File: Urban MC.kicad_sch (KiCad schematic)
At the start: 78 parts, among them J1 Conn_01x02, J2 Conn_01x02, J3 Conn_01x03, J4 Conn_01x02, Q1 IQE022N06LM5CGSCATMA1, Q10 IQE022N06LM5CGSCATMA1, Q11 IQE022N06LM5CGSCATMA1, Q12 IQE022N06LM5CGSCATMA1, Q13 IQE022N06LM5CGSCATMA1, Q14 IQE022N06LM5CGSCATMA1, Q15 IQE022N06LM5CGSCATMA1, Q16 IQE022N06LM5CGSCATMA1, Q17 IQE022N06LM5CGSCATMA1, Q18 IQE022N06LM5CGSCATMA1, Q19 IQE022N06LM5CGSCATMA1, Q2 IQE022N06LM5CGSCATMA1, Q20 IQE022N06LM5CGSCATMA1, Q21 IQE022N06LM5CGSCATMA1, Q22 IQE022N06LM5CGSCATMA1, Q23 IQE022N06LM5CGSCATMA1, Q24 IQE022N06LM5CGSCATMA1, Q3 IQE022N06LM5CGSCATMA1, Q4 IQE022N06LM5CGSCATMA1, Q5 IQE022N06LM5CGSCATMA1, Q6 IQE022N06LM5CGSCATMA1, Q7 IQE022N06LM5CGSCATMA1, Q8 IQE022N06LM5CGSCATMA1, Q9 IQE022N06LM5CGSCATMA1, SW1 CAN_TERM, SW2 SW_Push, U1 MCP2561/2, U1 MCP4725, U2 MCP2515-xSO, Y1 8MHz

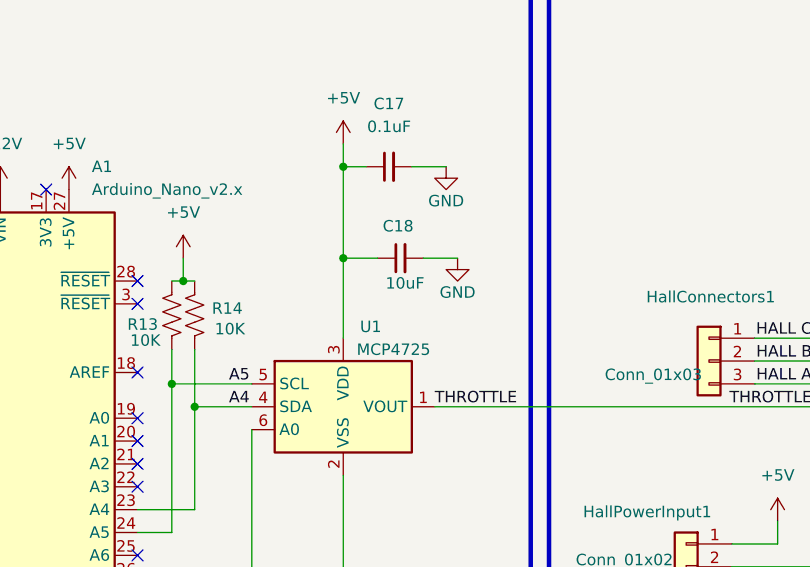
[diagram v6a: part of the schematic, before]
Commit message: all datasheets except CAN TERM and crystal
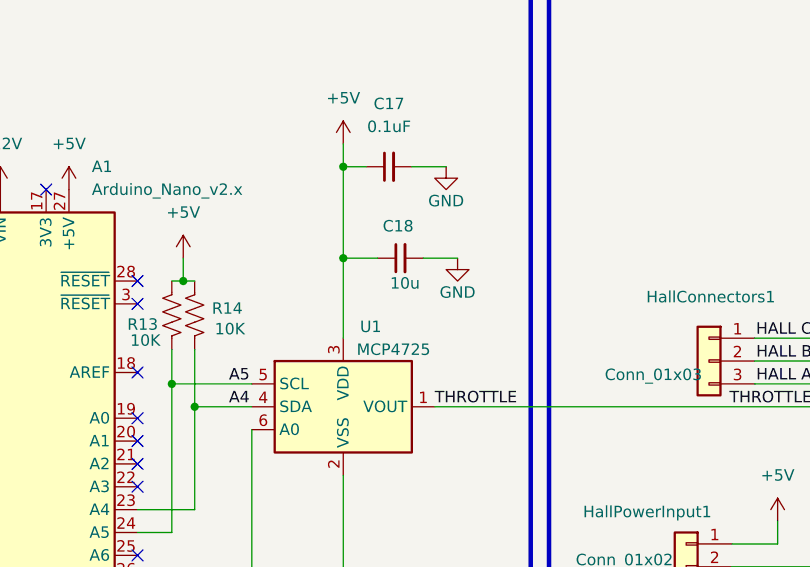
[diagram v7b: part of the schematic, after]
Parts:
- C18: value 10uF -> 10u; footprint Capacitor_SMD:C_0805_2012Metric_Pad1.18x1.45mm_HandSolder -> Capacitor_SMD:C_0805_2012Metric
- R4: footprint Resistor_SMD:R_0805_2012Metric_Pad1.20x1.40mm_HandSolder -> Resistor_SMD:R_0402_1005Metric
- SW2: footprint Button_Switch_THT:SW_PUSH_6mm -> urban_mc_custom_footprints:SW_TS04-66-70-BK-160-SMT
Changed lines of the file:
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@@
 			)
 		)
-		(property "Datasheet" "~"
+		(property "Datasheet" "https://www.molex.com/content/dam/molex/molex-dot-com/products/automated/en-us/salesdrawingpdf/436/43650/436500200_sd.pdf?inline"
 			(at 97.79 58.42 0)
 			(effects
@@
 			)
 		)
-		(property "Footprint" "Button_Switch_THT:SW_PUSH_6mm"
+		(property "Footprint" "urban_mc_custom_footprints:SW_TS04-66-70-BK-160-SMT"
 			(at 250.19 74.93 0)
 			(effects
@@
 			)
 		)
-		(property "Datasheet" "~"
+		(property "Datasheet" "https://www.sameskydevices.com/product/resource/ts04.pdf"
 			(at 250.19 74.93 0)
 			(effects
@@
 			)
 		)
-		(property "Datasheet" "~"
+		(property "Datasheet" "https://www.molex.com/content/dam/molex/molex-dot-com/products/automated/en-us/salesdrawingpdf/436/43650/436500200_sd.pdf?inline"
 			(at 201.93 102.87 0)
 			(effects
@@
 			)
 		)
-		(property "Datasheet" "~"
+		(property "Datasheet" "https://search.murata.co.jp/Ceramy/image/img/A01X/G101/ENG/GRM21BR61H106KE43-01A.pdf"
 			(at 308.61 72.39 0)
 			(effects
@@
 			)
 		)
-		(property "Datasheet" "~"
+		(property "Datasheet" "https://www.seielect.com/catalog/sei-rmcf_rmcp.pdf"
 			(at 76.2 59.69 0)
 			(effects
@@
 			)
 		)
-		(property "Datasheet" "~"
+		(property "Datasheet" "https://www.te.com/usa-en/product-1986660-2.datasheet.pdf"
 			(at 26.67 179.07 0)
 			(effects
@@
 			)
 		)
-		(property "Datasheet" "~"
+		(property "Datasheet" "https://search.murata.co.jp/Ceramy/image/img/A01X/G101/ENG/GRM21BR61H106KE43-01A.pdf"
 			(at 308.61 171.45 0)
 			(effects
@@
 			)
 		)
-		(property "Footprint" "Resistor_SMD:R_0805_2012Metric_Pad1.20x1.40mm_HandSolder"
+		(property "Footprint" "Resistor_SMD:R_0402_1005Metric"
 			(at 49.149 78.994 90)
 			(effects
@@
 			)
 		)
-		(property "Datasheet" "~"
+		(property "Datasheet" "https://industrial.panasonic.com/cdbs/www-data/pdf/RDA0000/AOA0000C304.pdf"
 			(at 48.895 80.01 0)
 			(effects
@@
 			)
 		)
-		(property "Datasheet" "~"
+		(property "Datasheet" "https://search.murata.co.jp/Ceramy/image/img/A01X/G101/ENG/GRM21BR61H106KE43-01A.pdf"
 			(at 308.61 123.19 0)
 			(effects
@@
 			)
 		)
-		(property "Datasheet" "~"
+		(property "Datasheet" "https://www.digikey.ca/en/products/detail/vishay-dale/CRCW040211R0FKED/1177783"
 			(at 313.69 67.31 0)
 			(effects
@@
 			)
 		)
-		(property "Datasheet" "~"
+		(property "Datasheet" "https://search.murata.co.jp/Ceramy/image/img/A01X/G101/ENG/GRM21BR61H106KE43-01A.pdf"
 			(at 285.75 165.1 0)
 			(effects
@@
 			)
 		)
-		(property "Datasheet" "~"
+		(property "Datasheet" "https://www.digikey.ca/en/products/detail/vishay-dale/CRCW040211R0FKED/1177783"
 			(at 308.61 82.55 0)
 			(effects
@@
 			)
 		)
-		(property "Value" "10uF"
+		(property "Value" "10u"
 			(at 170.688 73.914 90)
 			(effects
@@
 			)
 		)
-		(property "Footprint" "Capacitor_SMD:C_0805_2012Metric_Pad1.18x1.45mm_HandSolder"
+		(property "Footprint" "Capacitor_SMD:C_0805_2012Metric"
 			(at 170.18 71.12 0)
 			(effects
@@
 			)
 		)
-		(property "Datasheet" "https://search.murata.co.jp/Ceramy/image/img/A01X/G101/ENG/GRM21BR61C106KE15-01.pdf"
+		(property "Datasheet" "https://search.murata.co.jp/Ceramy/image/img/A01X/G101/ENG/GRM21BR61H106KE43-01A.pdf"
 			(at 170.18 71.12 0)
 			(effects
@@
 			)
 		)
-		(property "Datasheet" "~"
+		(property "Datasheet" "https://www.digikey.ca/en/products/detail/vishay-dale/CRCW040211R0FKED/1177783"
 			(at 313.69 118.11 0)
 			(effects
@@
 			)
 		)
-		(property "Datasheet" "~"
+		(property "Datasheet" "https://www.seielect.com/catalog/sei-rmcf_rmcp.pdf"
 			(at 320.04 72.39 0)
 			(effects
@@
 			)
 		)
-		(property "Datasheet" "~"
+		(property "Datasheet" "https://content.kemet.com/datasheets/KEM_C1003_C0G_SMD.pdf"
 			(at 33.02 119.38 0)
 			(effects
@@
 			)
 		)
-		(property "Datasheet" "~"
+		(property "Datasheet" "https://www.molex.com/content/dam/molex/molex-dot-com/products/automated/en-us/salesdrawingpdf/436/43650/436500200_sd.pdf?inline"
 			(at 97.79 64.77 0)
 			(effects
@@
 			)
 		)
-		(property "Datasheet" "~"
+		(property "Datasheet" "https://search.murata.co.jp/Ceramy/image/img/A01X/G101/ENG/GRM21BR61H106KE43-01A.pdf"
 			(at 243.84 48.26 0)
 			(effects
@@
 			)
 		)
-		(property "Datasheet" "~"
+		(property "Datasheet" "https://mm.digikey.com/Volume0/opasdata/d220001/medias/docus/658/CL31A226KAHNNNE_Spec.pdf"
 			(at 83.82 180.34 0)
 			(effects
@@
 			)
 		)
-		(property "Datasheet" "~"
+		(property "Datasheet" "https://industrial.panasonic.com/cdbs/www-data/pdf/RDA0000/AOA0000C304.pdf"
 			(at 144.78 77.47 0)
 			(effects
@@
 			)
 		)
-		(property "Datasheet" "~"
+		(property "Datasheet" "https://search.murata.co.jp/Ceramy/image/img/A01X/G101/ENG/GRM21BR61H106KE43-01A.pdf"
 			(at 38.1 180.34 0)
 			(effects
@@
 			)
 		)
-		(property "Datasheet" "~"
+		(property "Datasheet" "https://www.te.com/usa-en/product-1986660-3.datasheet.pdf"
 			(at 415.29 119.38 0)
 			(effects
@@
 			)
 		)
-		(property "Datasheet" "~"
+		(property "Datasheet" "https://industrial.panasonic.com/cdbs/www-data/pdf/RDA0000/AOA0000C304.pdf"
 			(at 218.44 96.52 0)
 			(effects
@@
 			)
 		)
-		(property "Datasheet" "~"
+		(property "Datasheet" "https://search.murata.co.jp/Ceramy/image/img/A01X/G101/ENG/GRM21BR61H106KE43-01A.pdf"
 			(at 285.75 116.84 0)
 			(effects
@@
 			)
 		)
-		(property "Datasheet" "~"
+		(property "Datasheet" "https://www.molex.com/content/dam/molex/molex-dot-com/products/automated/en-us/salesdrawingpdf/436/43650/436500300_sd.pdf?inline"
 			(at 204.47 82.55 0)
 			(effects
@@
 			)
 		)
-		(property "Datasheet" "~"
+		(property "Datasheet" "https://content.kemet.com/datasheets/KEM_C1003_C0G_SMD.pdf"
 			(at 33.02 127 0)
 			(effects
@@
 			)
 		)
-		(property "Datasheet" "~"
+		(property "Datasheet" "https://www.digikey.ca/en/products/detail/vishay-dale/CRCW040211R0FKED/1177783"
 			(at 313.69 166.37 0)
 			(effects
@@
 			)
 		)
-		(property "Datasheet" "http://ww1.microchip.com/downloads/en/devicedoc/21667d.pdf"
+		(property "Datasheet" "MCP2561/2 Data Sheet"
 			(at 57.15 64.77 0)
 			(effects
@@
 			)
 		)
-		(property "Datasheet" "~"
+		(property "Datasheet" "https://www.digikey.ca/en/products/detail/vishay-dale/CRCW040211R0FKED/1177783"
 			(at 308.61 181.61 0)
 			(effects
@@
 			)
 		)
-		(property "Datasheet" "~"
+		(property "Datasheet" "https://search.murata.co.jp/Ceramy/image/img/A01X/G101/ENG/GRM21BR61H106KE43-01A.pdf"
 			(at 285.75 66.04 0)
 			(effects
@@
 			)
 		)
-		(property "Datasheet" "~"
+		(property "Datasheet" "https://industrial.panasonic.com/cdbs/www-data/pdf/RDA0000/AOA0000C304.pdf"
 			(at 147.32 77.47 0)
 			(effects
@@
 			)
 		)
-		(property "Datasheet" "~"
+		(property "Datasheet" "https://www.seielect.com/catalog/sei-rmcf_rmcp.pdf"
 			(at 320.04 123.19 0)
 			(effects
@@
 			)
 		)
-		(property "Datasheet" "~"
+		(property "Datasheet" "https://www.seielect.com/catalog/sei-rmcf_rmcp.pdf"
 			(at 320.04 171.45 0)
 			(effects
@@
 			)
 		)
-		(property "Datasheet" "~"
+		(property "Datasheet" "https://product.tdk.com/system/files/dam/doc/product/capacitor/ceramic/mlcc/catalog/mlcc_commercial_general_en.pdf"
 			(at 48.26 180.34 0)
 			(effects
@@
 			)
 		)
-		(property "Datasheet" "~"
+		(property "Datasheet" "https://www.digikey.ca/en/products/detail/vishay-dale/CRCW040211R0FKED/1177783"
 			(at 308.61 133.35 0)
 			(effects
